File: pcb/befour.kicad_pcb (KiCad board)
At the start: 2 copper layers, 1 part

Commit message: more pcb work
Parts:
- added D1: D, Diode_THT:D_DO-35_SOD27_P7.62mm_Horizontal, F.Cu at (123.6, 102.3)
- added D2: D, Diode_THT:D_DO-35_SOD27_P7.62mm_Horizontal, F.Cu at (123.6, 105.8)
- added R1: 10k, Resistor_THT:R_Axial_DIN0207_L6.3mm_D2.5mm_P10.16mm_Horizontal, F.Cu at (98.4, 102.5)
- added SW1: SW_Push, Button_Switch_THT:SW_PUSH_6mm_H5mm, F.Cu at (157.6, 83.0)
- added SW2: SW_SPDT, Button_Switch_THT:SW_Slide_SPDT_Straight_CK_OS102011MS2Q, F.Cu at (114.1, 104.0)
- added U1: MEMORY, Package_DIP:DIP-28_W15.24mm, F.Cu at (62.8, 44.0)
- added U10: AREG, Package_DIP:DIP-16_W7.62mm_Socket, F.Cu at (134.1, 61.1)
- added U11: TEMP, Package_DIP:DIP-16_W7.62mm_Socket, F.Cu at (145.9, 61.1)
- added U12: BREG, Package_DIP:DIP-16_W7.62mm_Socket, F.Cu at (157.6, 61.1)
- added U2: 74LS125, Package_DIP:DIP-14_W7.62mm_Socket, F.Cu at (98.9, 83.1)
- added U3: 74LS125, Package_DIP:DIP-14_W7.62mm_Socket, F.Cu at (110.6, 83.1)
- added U4: 74LS374, Package_DIP:DIP-20_W7.62mm_Socket, F.Cu at (145.9, 83.1)
- added U5: 74LS14, Package_DIP:DIP-14_W7.62mm_Socket, F.Cu at (122.4, 83.1)
- added U6: 74LS138, Package_DIP:DIP-16_W7.62mm_Socket, F.Cu at (98.9, 61.1)
- added U7: 74LS161, Package_DIP:DIP-16_W7.62mm_Socket, F.Cu at (110.6, 61.1)
- added U8: 74LS11, Package_DIP:DIP-14_W7.62mm_Socket, F.Cu at (134.1, 83.1)
- added U9: 74LS138, Package_DIP:DIP-16_W7.62mm_Socket, F.Cu at (122.4, 61.1)
- added X1: 1MHz, Oscillator:Oscillator_DIP-14, F.Cu at (83.1, 52.8)

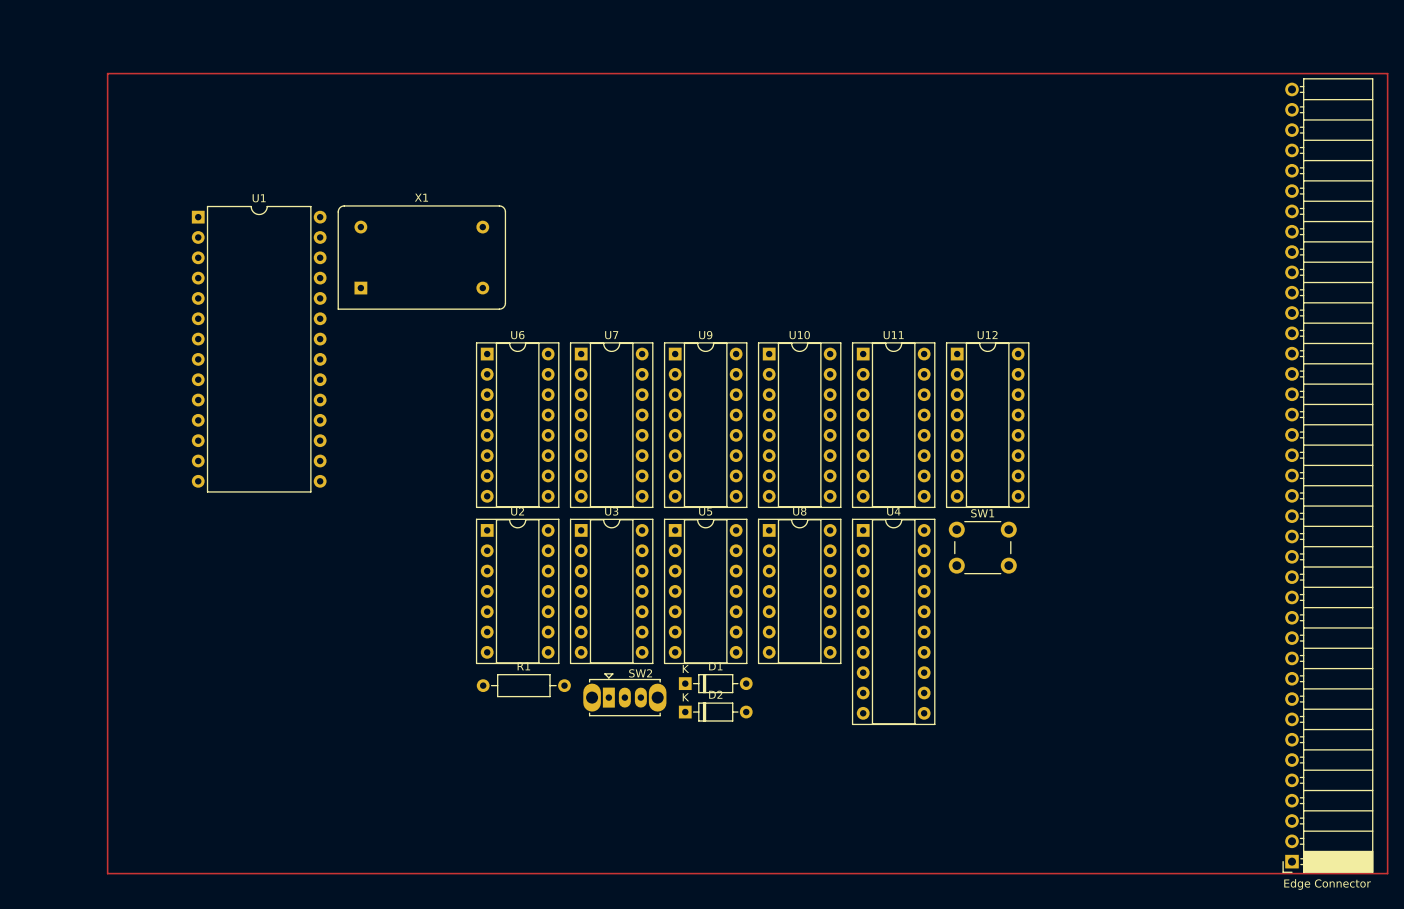
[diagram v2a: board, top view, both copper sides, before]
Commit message: the Schematic is complete.
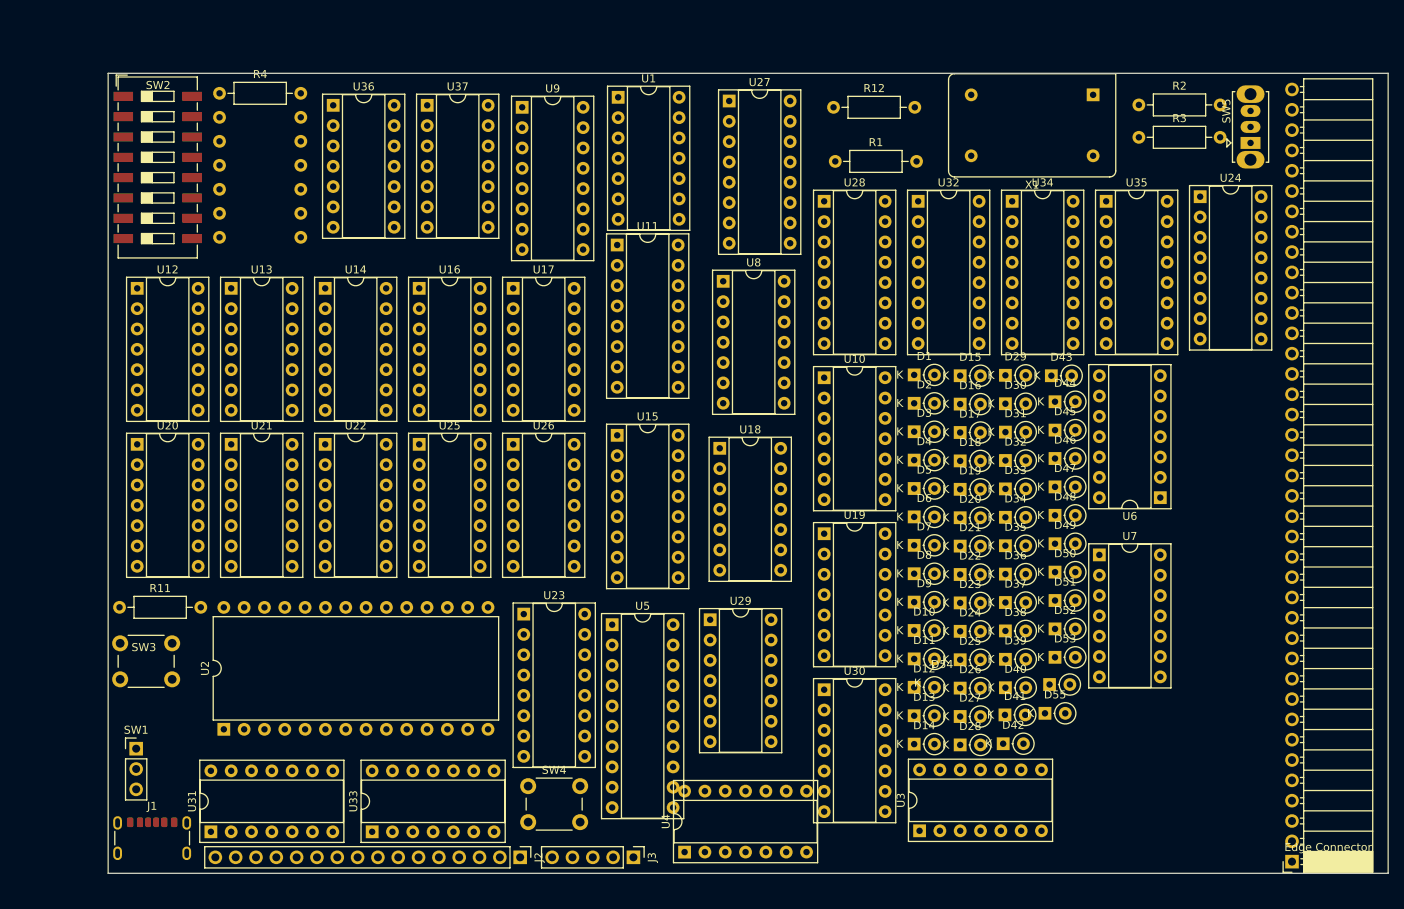
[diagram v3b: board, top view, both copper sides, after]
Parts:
- added D10: D, Diode_THT:D_DO-35_SOD27_P2.54mm_Vertical_KathodeUp, F.Cu at (152.2, 95.7)
- added D11: D, Diode_THT:D_DO-35_SOD27_P2.54mm_Vertical_KathodeUp, F.Cu at (152.2, 99.2)
- added D12: D, Diode_THT:D_DO-35_SOD27_P2.54mm_Vertical_KathodeUp, F.Cu at (152.2, 102.8)
- added D13: D, Diode_THT:D_DO-35_SOD27_P2.54mm_Vertical_KathodeUp, F.Cu at (152.2, 106.3)
- added D14: D, Diode_THT:D_DO-35_SOD27_P2.54mm_Vertical_KathodeUp, F.Cu at (152.2, 109.8)
- added D15: D, Diode_THT:D_DO-35_SOD27_P2.54mm_Vertical_KathodeUp, F.Cu at (158.0, 63.8)
- added D16: D, Diode_THT:D_DO-35_SOD27_P2.54mm_Vertical_KathodeUp, F.Cu at (158.0, 67.3)
- added D17: D, Diode_THT:D_DO-35_SOD27_P2.54mm_Vertical_KathodeUp, F.Cu at (158.0, 70.9)
- added D18: D, Diode_THT:D_DO-35_SOD27_P2.54mm_Vertical_KathodeUp, F.Cu at (158.0, 74.5)
- added D19: D, Diode_THT:D_DO-35_SOD27_P2.54mm_Vertical_KathodeUp, F.Cu at (158.0, 78.0)
- added D20: D, Diode_THT:D_DO-35_SOD27_P2.54mm_Vertical_KathodeUp, F.Cu at (158.0, 81.5)
- added D21: D, Diode_THT:D_DO-35_SOD27_P2.54mm_Vertical_KathodeUp, F.Cu at (158.0, 85.1)
- added D22: D, Diode_THT:D_DO-35_SOD27_P2.54mm_Vertical_KathodeUp, F.Cu at (158.0, 88.7)
- added D23: D, Diode_THT:D_DO-35_SOD27_P2.54mm_Vertical_KathodeUp, F.Cu at (158.0, 92.2)
- added D24: D, Diode_THT:D_DO-35_SOD27_P2.54mm_Vertical_KathodeUp, F.Cu at (158.0, 95.8)
- added D25: D, Diode_THT:D_DO-35_SOD27_P2.54mm_Vertical_KathodeUp, F.Cu at (158.0, 99.3)
- added D26: D, Diode_THT:D_DO-35_SOD27_P2.54mm_Vertical_KathodeUp, F.Cu at (158.0, 102.8)
- added D27: D, Diode_THT:D_DO-35_SOD27_P2.54mm_Vertical_KathodeUp, F.Cu at (158.0, 106.4)
- added D28: D, Diode_THT:D_DO-35_SOD27_P2.54mm_Vertical_KathodeUp, F.Cu at (158.0, 110.0)
- added D29: D, Diode_THT:D_DO-35_SOD27_P2.54mm_Vertical_KathodeUp, F.Cu at (163.7, 63.8)
- added D3: D, Diode_THT:D_DO-35_SOD27_P2.54mm_Vertical_KathodeUp, F.Cu at (152.2, 70.8)
- added D30: D, Diode_THT:D_DO-35_SOD27_P2.54mm_Vertical_KathodeUp, F.Cu at (163.7, 67.3)
- added D31: D, Diode_THT:D_DO-35_SOD27_P2.54mm_Vertical_KathodeUp, F.Cu at (163.7, 70.8)
- added D32: D, Diode_THT:D_DO-35_SOD27_P2.54mm_Vertical_KathodeUp, F.Cu at (163.7, 74.4)
- added D33: D, Diode_THT:D_DO-35_SOD27_P2.54mm_Vertical_KathodeUp, F.Cu at (163.7, 78.0)
- added D34: D, Diode_THT:D_DO-35_SOD27_P2.54mm_Vertical_KathodeUp, F.Cu at (163.7, 81.5)
- added D35: D, Diode_THT:D_DO-35_SOD27_P2.54mm_Vertical_KathodeUp, F.Cu at (163.7, 85.0)
- added D36: D, Diode_THT:D_DO-35_SOD27_P2.54mm_Vertical_KathodeUp, F.Cu at (163.7, 88.6)
- added D37: D, Diode_THT:D_DO-35_SOD27_P2.54mm_Vertical_KathodeUp, F.Cu at (163.7, 92.2)
- added D38: D, Diode_THT:D_DO-35_SOD27_P2.54mm_Vertical_KathodeUp, F.Cu at (163.7, 95.7)
- added D39: D, Diode_THT:D_DO-35_SOD27_P2.54mm_Vertical_KathodeUp, F.Cu at (163.7, 99.2)
- added D4: D, Diode_THT:D_DO-35_SOD27_P2.54mm_Vertical_KathodeUp, F.Cu at (152.2, 74.3)
- added D40: D, Diode_THT:D_DO-35_SOD27_P2.54mm_Vertical_KathodeUp, F.Cu at (163.7, 102.8)
- added D41: D, Diode_THT:D_DO-35_SOD27_P2.54mm_Vertical_KathodeUp, F.Cu at (163.6, 106.2)
- added D42: D, Diode_THT:D_DO-35_SOD27_P2.54mm_Vertical_KathodeUp, F.Cu at (163.4, 109.8)
- added D43: D, Diode_THT:D_DO-35_SOD27_P2.54mm_Vertical_KathodeUp, F.Cu at (169.4, 63.8)
- added D44: D, Diode_THT:D_DO-35_SOD27_P2.54mm_Vertical_KathodeUp, F.Cu at (169.9, 67.0)
- added D45: D, Diode_THT:D_DO-35_SOD27_P2.54mm_Vertical_KathodeUp, F.Cu at (169.9, 70.6)
- added D46: D, Diode_THT:D_DO-35_SOD27_P2.54mm_Vertical_KathodeUp, F.Cu at (169.9, 74.2)
- added D47: D, Diode_THT:D_DO-35_SOD27_P2.54mm_Vertical_KathodeUp, F.Cu at (169.9, 77.7)
- added D48: D, Diode_THT:D_DO-35_SOD27_P2.54mm_Vertical_KathodeUp, F.Cu at (169.9, 81.2)
- added D49: D, Diode_THT:D_DO-35_SOD27_P2.54mm_Vertical_KathodeUp, F.Cu at (169.9, 84.8)
- added D5: D, Diode_THT:D_DO-35_SOD27_P2.54mm_Vertical_KathodeUp, F.Cu at (152.2, 77.9)
- added D50: D, Diode_THT:D_DO-35_SOD27_P2.54mm_Vertical_KathodeUp, F.Cu at (169.9, 88.3)
- added D51: D, Diode_THT:D_DO-35_SOD27_P2.54mm_Vertical_KathodeUp, F.Cu at (169.9, 91.9)
- added D52: D, Diode_THT:D_DO-35_SOD27_P2.54mm_Vertical_KathodeUp, F.Cu at (169.9, 95.5)
- added D53: D, Diode_THT:D_DO-35_SOD27_P2.54mm_Vertical_KathodeUp, F.Cu at (169.9, 99.0)
- added D54: D, Diode_THT:D_DO-35_SOD27_P2.54mm_Vertical_KathodeUp, F.Cu at (169.2, 102.4)
- added D55: D, Diode_THT:D_DO-35_SOD27_P2.54mm_Vertical_KathodeUp, F.Cu at (168.6, 106.0)
- added D6: D, Diode_THT:D_DO-35_SOD27_P2.54mm_Vertical_KathodeUp, F.Cu at (152.2, 81.5)
- added D7: D, Diode_THT:D_DO-35_SOD27_P2.54mm_Vertical_KathodeUp, F.Cu at (152.2, 85.0)
- added D8: D, Diode_THT:D_DO-35_SOD27_P2.54mm_Vertical_KathodeUp, F.Cu at (152.2, 88.5)
- added D9: D, Diode_THT:D_DO-35_SOD27_P2.54mm_Vertical_KathodeUp, F.Cu at (152.2, 92.1)
- added J1: USB, Connector_USB:USB_C_Receptacle_GCT_USB4125-xx-x_6P_TopMnt_Horizontal, F.Cu at (57.0, 122.7)
- added J2: READOUT, Connector_PinHeader_2.54mm:PinHeader_1x16_P2.54mm_Vertical, F.Cu at (103.0, 124.0)
- added J3: DEVICES, Connector_PinHeader_2.54mm:PinHeader_1x05_P2.54mm_Vertical, F.Cu at (117.2, 124.0)
- added R10: 10K, Resistor_THT:R_Axial_DIN0207_L6.3mm_D2.5mm_P10.16mm_Horizontal, B.Cu at (65.4, 46.5)
- added R11: 10k, Resistor_THT:R_Axial_DIN0207_L6.3mm_D2.5mm_P10.16mm_Horizontal, F.Cu at (52.9, 92.8)
- added R12: 10k, Resistor_THT:R_Axial_DIN0207_L6.3mm_D2.5mm_P10.16mm_Horizontal, F.Cu at (142.2, 30.2)
- added R2: 5.1K, Resistor_THT:R_Axial_DIN0207_L6.3mm_D2.5mm_P10.16mm_Horizontal, F.Cu at (180.3, 29.9)
- added R3: 5.1K, Resistor_THT:R_Axial_DIN0207_L6.3mm_D2.5mm_P10.16mm_Horizontal, F.Cu at (180.3, 34.0)
- added R4: 10K, Resistor_THT:R_Axial_DIN0207_L6.3mm_D2.5mm_P10.16mm_Horizontal, F.Cu at (65.4, 28.5)
- added R5: 10K, Resistor_THT:R_Axial_DIN0207_L6.3mm_D2.5mm_P10.16mm_Horizontal, B.Cu at (65.4, 31.5)
- added R6: 10K, Resistor_THT:R_Axial_DIN0207_L6.3mm_D2.5mm_P10.16mm_Horizontal, B.Cu at (65.4, 34.5)
- added R7: 10K, Resistor_THT:R_Axial_DIN0207_L6.3mm_D2.5mm_P10.16mm_Horizontal, B.Cu at (65.4, 37.5)
- added R8: 10K, Resistor_THT:R_Axial_DIN0207_L6.3mm_D2.5mm_P10.16mm_Horizontal, B.Cu at (65.4, 40.5)
- added R9: 10K, Resistor_THT:R_Axial_DIN0207_L6.3mm_D2.5mm_P10.16mm_Horizontal, B.Cu at (65.4, 43.5)
- added SW3: SW_Push, Button_Switch_THT:SW_PUSH_6mm_H5mm, F.Cu at (53.0, 97.2)
- added SW4: SW_Push, Button_Switch_THT:SW_PUSH_6mm_H5mm, F.Cu at (104.0, 115.1)
- added SW5: SW_SPDT, Button_Switch_THT:SW_Slide_SPDT_Straight_CK_OS102011MS2Q, F.Cu at (194.3, 34.7)
- added U13: SI_BUFFER, Package_DIP:DIP-14_W7.62mm_Socket, F.Cu at (66.9, 52.9)
- added U14: 74LS00, Package_DIP:DIP-14_W7.62mm_Socket, F.Cu at (78.6, 52.9)
- added U15: CLKDIV, Package_DIP:DIP-16_W7.62mm_Socket, F.Cu at (115.1, 71.2)
- added U16: 74LS14, Package_DIP:DIP-14_W7.62mm_Socket, F.Cu at (90.4, 52.9)
- added U17: MISC, Package_DIP:DIP-14_W7.62mm_Socket, F.Cu at (102.1, 52.9)
- added U18: ALU_NAND_BUFFER, Package_DIP:DIP-14_W7.62mm_Socket, F.Cu at (128.0, 72.9)
- added U19: 74LS11, Package_DIP:DIP-14_W7.62mm_Socket, F.Cu at (141.0, 83.5)
- added U20: 74LS11, Package_DIP:DIP-14_W7.62mm_Socket, F.Cu at (55.1, 72.4)
- added U21: A_BUFFER, Package_DIP:DIP-14_W7.62mm_Socket, F.Cu at (66.9, 72.4)
- added U22: ALU_ADD_BUFFER, Package_DIP:DIP-14_W7.62mm_Socket, F.Cu at (78.6, 72.4)
- added U23: CLKDIV2, Package_DIP:DIP-16_W7.62mm_Socket, F.Cu at (103.5, 93.6)
- added U24: AREG, Package_DIP:DIP-16_W7.62mm_Socket, F.Cu at (188.0, 41.4)
- added U25: 74LS00, Package_DIP:DIP-14_W7.62mm_Socket, F.Cu at (90.4, 72.4)
- added U26: XOR_EQUAL, Package_DIP:DIP-14_W7.62mm_Socket, F.Cu at (102.1, 72.4)
- added U27: TEMP, Package_DIP:DIP-16_W7.62mm_Socket, F.Cu at (129.1, 29.5)
- added U28: BREG, Package_DIP:DIP-16_W7.62mm_Socket, F.Cu at (141.0, 42.0)
- added U29: FLAGS_BUFFER, Package_DIP:DIP-14_W7.62mm_Socket, F.Cu at (126.8, 94.3)
- added U30: DEVICES_BUFFER, Package_DIP:DIP-14_W7.62mm_Socket, F.Cu at (141.0, 103.0)
- added U31: PCH_BUFFER, Package_DIP:DIP-14_W7.62mm_Socket, F.Cu at (64.3, 120.8)
- added U32: 74LS138, Package_DIP:DIP-16_W7.62mm_Socket, F.Cu at (152.8, 42.0)
- added U33: PCL_BUFFER, Package_DIP:DIP-14_W7.62mm_Socket, F.Cu at (84.5, 120.8)
- added U34: PCH, Package_DIP:DIP-16_W7.62mm_Socket, F.Cu at (164.5, 42.0)
- added U35: PCL, Package_DIP:DIP-16_W7.62mm_Socket, F.Cu at (176.2, 42.0)
- added U36: ADR_BUFFER, Package_DIP:DIP-14_W7.62mm_Socket, F.Cu at (79.6, 30.0)
- added U37: SI_ADR_BUFFER, Package_DIP:DIP-14_W7.62mm_Socket, F.Cu at (91.4, 30.0)
- D1, D2: footprint Diode_THT:D_DO-35_SOD27_P7.62mm_Horizontal -> Diode_THT:D_DO-35_SOD27_P2.54mm_Vertical_KathodeUp
- R1: value 10k -> 1k
- SW1: value SW_Push -> SW_SPDT; footprint Button_Switch_THT:SW_PUSH_6mm_H5mm -> Connector_PinHeader_2.54mm:PinHeader_1x03_P2.54mm_Vertical
- SW2: value SW_SPDT -> PRG_SELECT; footprint Button_Switch_THT:SW_Slide_SPDT_Straight_CK_OS102011MS2Q -> Button_Switch_SMD:SW_DIP_SPSTx08_Slide_9.78x22.5mm_W8.61mm_P2.54mm
- U1: value MEMORY -> 74LS14; footprint Package_DIP:DIP-28_W15.24mm -> Package_DIP:DIP-14_W7.62mm_Socket
- U10: value AREG -> 74LS11; footprint Package_DIP:DIP-16_W7.62mm_Socket -> Package_DIP:DIP-14_W7.62mm_Socket
- U11: value TEMP -> ALU_ADD
- U12: value BREG -> ALU_NAND; footprint Package_DIP:DIP-16_W7.62mm_Socket -> Package_DIP:DIP-14_W7.62mm_Socket
- U2: value 74LS125 -> MEMORY; footprint Package_DIP:DIP-14_W7.62mm_Socket -> Package_DIP:DIP-28_W15.24mm
- U3: value 74LS125 -> B_OUT_BUFFER
- U4: value 74LS374 -> DB_OUT_BUFFER; footprint Package_DIP:DIP-20_W7.62mm_Socket -> Package_DIP:DIP-14_W7.62mm_Socket
- U5: value 74LS14 -> INSTSTORe; footprint Package_DIP:DIP-14_W7.62mm_Socket -> Package_DIP:DIP-20_W7.62mm_Socket
- U6: value 74LS138 -> TEMP_BUFFER; footprint Package_DIP:DIP-16_W7.62mm_Socket -> Package_DIP:DIP-14_W7.62mm_Socket
- U7: value 74LS161 -> B_BUFFER; footprint Package_DIP:DIP-16_W7.62mm_Socket -> Package_DIP:DIP-14_W7.62mm_Socket
- U8: value 74LS11 -> 74LS125
- moved SW1 106.2 mm to (55.0, 110.4)
- moved U12 102.8 mm to (55.1, 52.9)
- moved X1 94.7 mm to (174.6, 28.7), turned to 180 degrees
- moved SW2 87.0 mm to (57.7, 37.8)
- moved U6 86.0 mm to (183.0, 79.0), turned to 180 degrees
- moved R1 78.9 mm to (142.4, 37.0)
- moved U7 69.5 mm to (175.4, 86.2)
- moved U3 56.6 mm to (152.9, 120.7), turned to 90 degrees
- moved U1 54.6 mm to (115.2, 29.0)
- moved D1 48.0 mm to (152.2, 63.7)
- moved D2 48.0 mm to (152.2, 67.2)
- moved U4 46.0 mm to (123.6, 123.3), turned to 90 degrees
- moved U2 41.3 mm to (66.0, 108.0), turned to 90 degrees
- moved U9 36.3 mm to (103.2, 30.2)
- moved U11 33.6 mm to (115.1, 47.5)
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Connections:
- R1 pad 1: Net-(SW2-A) -> Net-(SW1-C)
- R1 pad 2: +5V -> GND
- SW1 pad 1: GND -> Net-(SW1-A)
- SW1 pad 2: Net-(SW2-A) -> +5V
- SW2 pad 1: Net-(SW2-A) -> +5V
- SW2 pad 2: Net-(SW2-B) -> +5V
- SW2 pad 3: CLK -> +5V
- U1 pad 1: GND -> WRITE
- U1 pad 10: unconnected-(U1-A0-Pad10) -> nLDINST
- U1 pad 11: /D0 -> LDINST
- U1 pad 12: /D1 -> Net-(U34-CEP)
- U1 pad 13: /D2 -> PerformJump
- U1 pad 14: GND -> +5V
- U1 pad 2: GND -> Net-(U2-~{OE})
- U1 pad 3: unconnected-(U1-A7-Pad3) -> AB
- U1 pad 4: unconnected-(U1-A6-Pad4) -> nAB
- U1 pad 5: unconnected-(U1-A5-Pad5) -> Net-(D40-K)
- U1 pad 6: unconnected-(U1-A4-Pad6) -> Net-(D46-A)
- U1 pad 7: unconnected-(U1-A3-Pad7) -> GND
- U1 pad 8: unconnected-(U1-A2-Pad8) -> Net-(U1-Pad8)
- U1 pad 9: unconnected-(U1-A1-Pad9) -> /Inst1
- U10 pad 1: RESET -> LD
- U10 pad 10: GND -> outputB
- U10 pad 11: /AOUT3 -> outputA
- U10 pad 12: /AOUT2 -> Net-(D22-A)
- U10 pad 13: /AOUT1 -> LDI
- U10 pad 14: /AOUT0 -> +5V
- U10 pad 2: CLK -> LD
- U10 pad 3: /DATABUS0 -> OP1
- U10 pad 4: /DATABUS1 -> +5V
- U10 pad 5: /DATABUS2 -> OP2
- U10 pad 6: /DATABUS3 -> OPERATION
- U10 pad 8: GND -> Net-(U10-Pad8)
- U10 pad 9: writeA -> outputLI
- U11 pad 1: RESET -> Net-(U11-S2)
- U11 pad 10: GND -> Net-(U11-S4)
- U11 pad 11: /TEMPOUT3 -> /DB3
- U11 pad 12: /TEMPOUT2 -> SignFlag
- U11 pad 13: /TEMPOUT1 -> Net-(U11-S3)
- U11 pad 14: /TEMPOUT0 -> /AOUT2
- U11 pad 15: unconnected-(U11-TC-Pad15) -> /DB2
- U11 pad 2: OP1^ -> /DB1
- U11 pad 3: /DATABUS0 -> /AOUT1
- U11 pad 4: /DATABUS1 -> Net-(U11-S1)
- U11 pad 5: /DATABUS2 -> /AOUT0
- U11 pad 6: /DATABUS3 -> /DB0
- U11 pad 7: GND -> CIN
- U11 pad 9: ALUOP -> COUT
- U12 pad 1: RESET -> /AOUT0
- U12 pad 10: GND -> /DB2
- U12 pad 11: /BOUT3 -> Net-(U12-Pad11)
- U12 pad 12: /BOUT2 -> SignFlag
- U12 pad 13: /BOUT1 -> /DB3
- U12 pad 14: /BOUT0 -> +5V
- U12 pad 2: CLK -> /DB0
- U12 pad 3: /DATABUS0 -> Net-(U12-Pad3)
- U12 pad 4: /DATABUS1 -> /AOUT1
- U12 pad 5: /DATABUS2 -> /DB1
- U12 pad 6: /DATABUS3 -> Net-(U12-Pad6)
- U12 pad 8: GND -> Net-(U12-Pad8)
- U12 pad 9: writeB -> /AOUT2
- U2 pad 1: WRITE -> Net-(U2-A14)
- U2 pad 10: WRITE -> /A0
- U2 pad 11: /ROM3 -> /D0
- U2 pad 12: /BOUT3 -> /D1
- U2 pad 13: WRITE -> /D2
- U2 pad 14: +5V -> GND
- U2 pad 2: /BOUT0 -> Net-(U2-A12)
- U2 pad 3: /ROM0 -> /A7
- U2 pad 4: WRITE -> /A6
- U2 pad 5: /BOUT1 -> /A5
- U2 pad 6: /ROM1 -> /A4
- U2 pad 7: GND -> /A3
- U2 pad 8: /ROM2 -> /A2
- U2 pad 9: /BOUT2 -> /A1
- U3 pad 11: /ROM7 -> /D3
- U3 pad 12: /DATABUS3 -> /BOUT3
- U3 pad 2: /DATABUS0 -> /BOUT0
- U3 pad 3: /ROM4 -> /D0
- U3 pad 5: /DATABUS1 -> /BOUT1
- U3 pad 6: /ROM5 -> /D1
- U3 pad 8: /ROM6 -> /D2
- U3 pad 9: /DATABUS2 -> /BOUT2
- U4 pad 1: GND -> WRITE
- U4 pad 10: GND -> WRITE
- U4 pad 11: nLDINST -> /D7
- U4 pad 12: /SI0 -> /DB3
- U4 pad 13: /D4 -> WRITE
- U4 pad 14: /D5 -> +5V
- U4 pad 2: Net-(U4-O0) -> /DB0
- U4 pad 3: /D0 -> /D4
- U4 pad 4: /D1 -> WRITE
- U4 pad 5: Net-(U4-O1) -> /DB1
- U4 pad 6: Net-(U4-O2) -> /D5
- U4 pad 7: /D2 -> GND
- U4 pad 8: /D3 -> /D6
- U4 pad 9: AB -> /DB2
- U5 pad 1: WRITE -> GND
- U5 pad 10: nLDINST -> GND
- U5 pad 11: LDINST -> nLDINST
- U5 pad 12: unconnected-(U5-Pad12) -> /SI0
- U5 pad 13: unconnected-(U5-Pad13) -> /D4
- U5 pad 14: +5V -> /D5
- U5 pad 2: Net-(U1-~{OE}) -> /Inst0
- U5 pad 3: unconnected-(U5-Pad3) -> /D0
- U5 pad 4: unconnected-(U5-Pad4) -> /D1
- U5 pad 5: unconnected-(U5-Pad5) -> /Inst1
- U5 pad 6: unconnected-(U5-Pad6) -> /Inst2
- U5 pad 7: GND -> /D2
- U5 pad 8: unconnected-(U5-Pad8) -> /D3
- U5 pad 9: unconnected-(U5-Pad9) -> AB
- U6 pad 1: Net-(U4-O0) -> outputTEMP
- U6 pad 10: ST -> outputB
- U6 pad 11: CMP -> /DB0
- U6 pad 12: NAND -> /BOUT0
- U6 pad 13: ADD -> outputB
- U6 pad 14: LD -> +5V
- U6 pad 2: Net-(U4-O1) -> /TEMPOUT3
- U6 pad 3: Net-(U4-O2) -> /DB3
- U6 pad 4: RESET -> outputTEMP
- U6 pad 5: GND -> /TEMPOUT2
- U6 pad 6: +5V -> /DB2
- U6 pad 7: JPC -> GND
- U6 pad 8: GND -> /DB1
- U6 pad 9: JP -> /BOUT1
- U7 pad 1: RESET -> outputB
- U7 pad 10: +5V -> outputTEMP
- U7 pad 11: unconnected-(U7-Q3-Pad11) -> /DB0
- U7 pad 12: unconnected-(U7-Q2-Pad12) -> /TEMPOUT0
- U7 pad 13: Net-(U7-Q1) -> outputTEMP
- U7 pad 14: Net-(U7-Q0) -> +5V
- U7 pad 2: Net-(SW2-B) -> /BOUT3
- U7 pad 3: GND -> /DB3
- U7 pad 4: GND -> outputB
- U7 pad 5: GND -> /BOUT2
- U7 pad 6: GND -> /DB2
- U7 pad 7: +5V -> GND
- U7 pad 8: GND -> /DB1
- U7 pad 9: +5V -> /TEMPOUT1
- U8 pad 1: NAND -> outputLI
- U8 pad 10: unconnected-(U8-Pad10) -> outputLI
- U8 pad 11: unconnected-(U8-Pad11) -> /DB0
- U8 pad 12: ALUOP -> /D4
- U8 pad 13: ADD -> outputLI
- U8 pad 2: +5V -> /D7
- U8 pad 3: LD -> /DB3
- U8 pad 4: +5V -> outputLI
- U8 pad 5: ST -> /D6
- U8 pad 6: ADDRESSING -> /DB2
- U8 pad 8: unconnected-(U8-Pad8) -> /DB1
- U8 pad 9: unconnected-(U8-Pad9) -> /D5
- U9 pad 1: Net-(U7-Q0) -> /Inst0
- U9 pad 10: unconnected-(U9-O5-Pad10) -> ST
- U9 pad 11: unconnected-(U9-O4-Pad11) -> CMP
- U9 pad 12: INCPC -> NAND
- U9 pad 13: OP2 -> ADD
- U9 pad 14: OP1 -> LD
- U9 pad 15: LDINST -> LDI
- U9 pad 2: Net-(U7-Q1) -> /Inst1
- U9 pad 3: GND -> /Inst2
- U9 pad 7: unconnected-(U9-O7-Pad7) -> JPC
- U9 pad 9: unconnected-(U9-O6-Pad9) -> JP
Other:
- board outline added: 160 x 100 mm

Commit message: schematic tweaks
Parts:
- removed Edge Connector: PinSocket_1x39_P2.54mm_Horizontal, Connector_PinSocket_2.54mm:PinSocket_1x39_P2.54mm_Horizontal
- added J5: Conn_01x40_Pin, Connector_PinHeader_2.54mm:PinHeader_1x40_P2.54mm_Horizontal, F.Cu at (201.0, 28.0)
- J1: value USB -> USB_C_Receptacle_PowerOnly_6P
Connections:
- R10 pad 1: Net-(U2-A14) -> A14
- R4 pad 1: Net-(U2-A8) -> A8
- R5 pad 1: Net-(U2-A9) -> A9
- R6 pad 1: Net-(U2-A10) -> A10
- R7 pad 1: Net-(U2-A11) -> A11
- R8 pad 1: Net-(U2-A12) -> A12
- R9 pad 1: Net-(U2-A13) -> A13
- SW5 pad 1: Net-(SW5-A) -> MANUALCLK
- U2 pad 1: Net-(U2-A14) -> A14
- U2 pad 2: Net-(U2-A12) -> A12
- U2 pad 21: Net-(U2-A10) -> A10
- U2 pad 23: Net-(U2-A11) -> A11
- U2 pad 24: Net-(U2-A9) -> A9
- U2 pad 25: Net-(U2-A8) -> A8
- U2 pad 26: Net-(U2-A13) -> A13

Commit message: PCB
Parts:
- removed J2: READOUT, Connector_PinHeader_2.54mm:PinHeader_1x16_P2.54mm_Vertical
- removed J3: DEVICES, Connector_PinHeader_2.54mm:PinHeader_1x05_P2.54mm_Vertical
- removed SW2: PRG_SELECT, Button_Switch_SMD:SW_DIP_SPSTx08_Slide_9.78x22.5mm_W8.61mm_P2.54mm
- removed SW3, SW4: SW_Push, Button_Switch_THT:SW_PUSH_6mm_H5mm
- removed U36: ADR_BUFFER, Package_DIP:DIP-14_W7.62mm_Socket
- added R13: 10K, Resistor_THT:R_Axial_DIN0309_L9.0mm_D3.2mm_P2.54mm_Vertical, F.Cu at (71.1, 110.7)
- added R14: 10K, Resistor_THT:R_Axial_DIN0309_L9.0mm_D3.2mm_P2.54mm_Vertical, F.Cu at (71.1, 106.7)
- R1, R2, R3, R4: footprint Resistor_THT:R_Axial_DIN0207_L6.3mm_D2.5mm_P10.16mm_Horizontal -> Resistor_THT:R_Axial_DIN0309_L9.0mm_D3.2mm_P2.54mm_Vertical
- R10, R5, R6, R7, R8, R9: footprint Resistor_THT:R_Axial_DIN0207_L6.3mm_D2.5mm_P10.16mm_Horizontal -> Resistor_THT:R_Axial_DIN0309_L9.0mm_D3.2mm_P2.54mm_Vertical; moved to F.Cu
- R11, R12: value 10k -> 10K; footprint Resistor_THT:R_Axial_DIN0207_L6.3mm_D2.5mm_P10.16mm_Horizontal -> Resistor_THT:R_Axial_DIN0309_L9.0mm_D3.2mm_P2.54mm_Vertical
- moved J5 177.2 mm to (50.8, 122.0), turned to 180 degrees
- moved J1 168.5 mm to (193.8, 24.3), turned to 180 degrees
- moved SW1 158.3 mm to (193.0, 33.0), turned to 90 degrees
- moved D45 119.3 mm to (61.0, 119.4), turned to 90 degrees
- moved D44 118.5 mm to (63.5, 119.4), turned to 90 degrees
- moved D43 117.3 mm to (63.5, 114.3), turned to 90 degrees
- moved U35 117.3 mm to (61.0, 63.5)
- moved X1 116.2 mm to (58.4, 31.8), turned to 0 degrees
- moved SW5 114.1 mm to (80.8, 22.9), turned to 0 degrees
- moved R12 110.4 mm to (71.1, 114.8), turned to 180 degrees
- moved D47 105.0 mm to (73.7, 35.6), turned to -90 degrees
- moved U34 103.5 mm to (61.0, 40.6)
- moved U16 103.5 mm to (180.3, 104.1)
- moved D40 102.9 mm to (61.0, 109.2), turned to 90 degrees
- moved D42 102.5 mm to (61.0, 114.3), turned to 90 degrees
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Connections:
- net MANUALCLK renamed EXTCLK
- J5 pad 29: DATAENTRY -> unconnected-(J5-Pin_29-Pad29)
- R11 pad 1: RESET -> +5V
- R11 pad 2: +5V -> /A7
- R12 pad 1: Net-(SW5-A) -> +5V
- R12 pad 2: +5V -> /A6
- U17 pad 1: Net-(U16-Pad4) -> ADD
- U17 pad 2: Net-(U12-Pad3) -> COUT
- U17 pad 3: /ALU0 -> Net-(D20-A)
- U18 pad 1: ADD -> Net-(U16-Pad4)
- U18 pad 2: COUT -> Net-(U12-Pad3)
- U18 pad 3: Net-(D20-A) -> /ALU0
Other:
- board size 160 x 100 mm -> 160 x 102.9 mm
